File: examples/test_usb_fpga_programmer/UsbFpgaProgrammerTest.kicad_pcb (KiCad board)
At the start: 2 copper layers, 52 x 18 mm, 38 parts

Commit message: ferrite bead
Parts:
- 0FB1: renamed from 0R3; footprint Resistor_SMD:R_0603_1608Metric -> Inductor_SMD:L_0603_1608Metric
- 0FB2: renamed from 0R4; footprint Resistor_SMD:R_0603_1608Metric -> Inductor_SMD:L_0603_1608Metric
- 0FB3: renamed from 0R5; footprint Resistor_SMD:R_0603_1608Metric -> Inductor_SMD:L_0603_1608Metric
- moved 0H1 28.6 mm to (124.0, 54.0)
- moved 0H3 28.2 mm to (150.0, 42.0)
- moved 0H2 1.41 mm to (150.0, 54.0)
- renumbered 0R6 to 0R3, 0R7 to 0R4, 0R8 to 0R5, 0R9 to 0R6, 0R10 to 0R7, 0R11 to 0R8

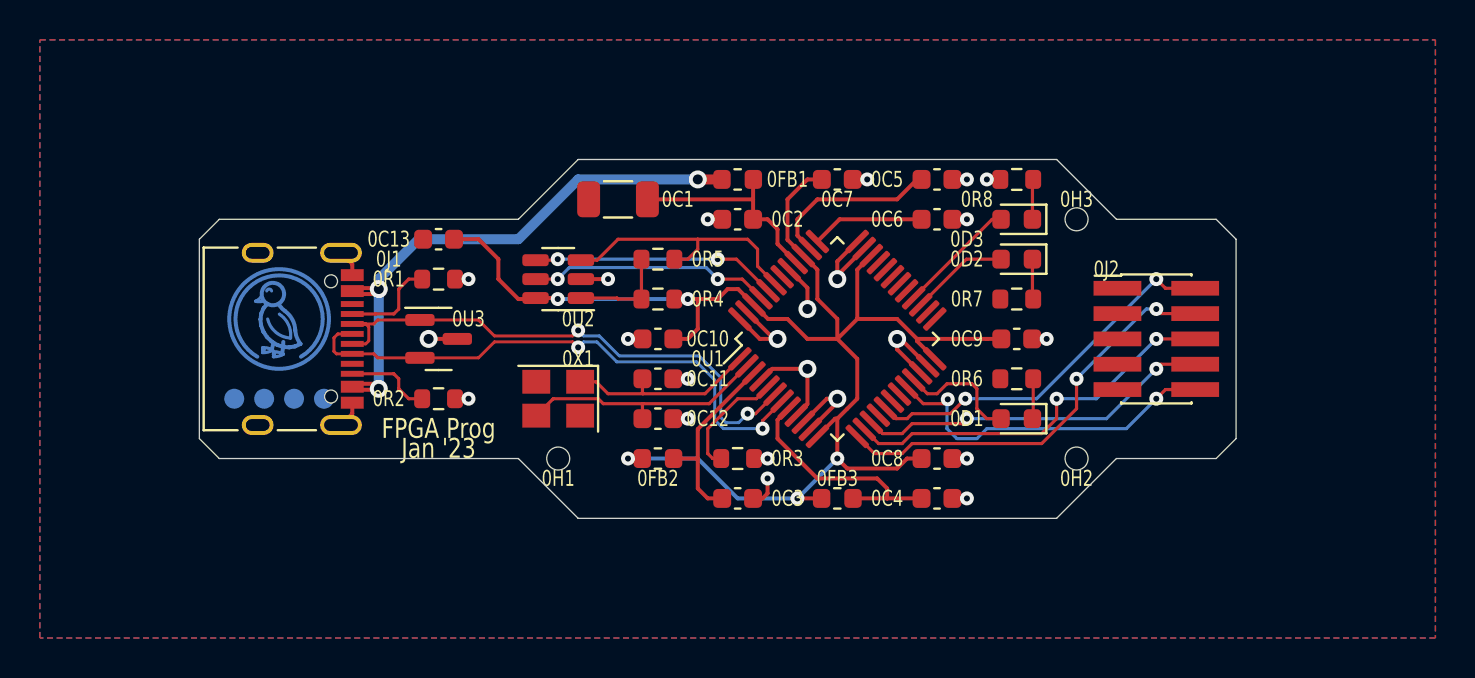
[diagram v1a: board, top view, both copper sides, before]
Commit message: leds and protection diodes
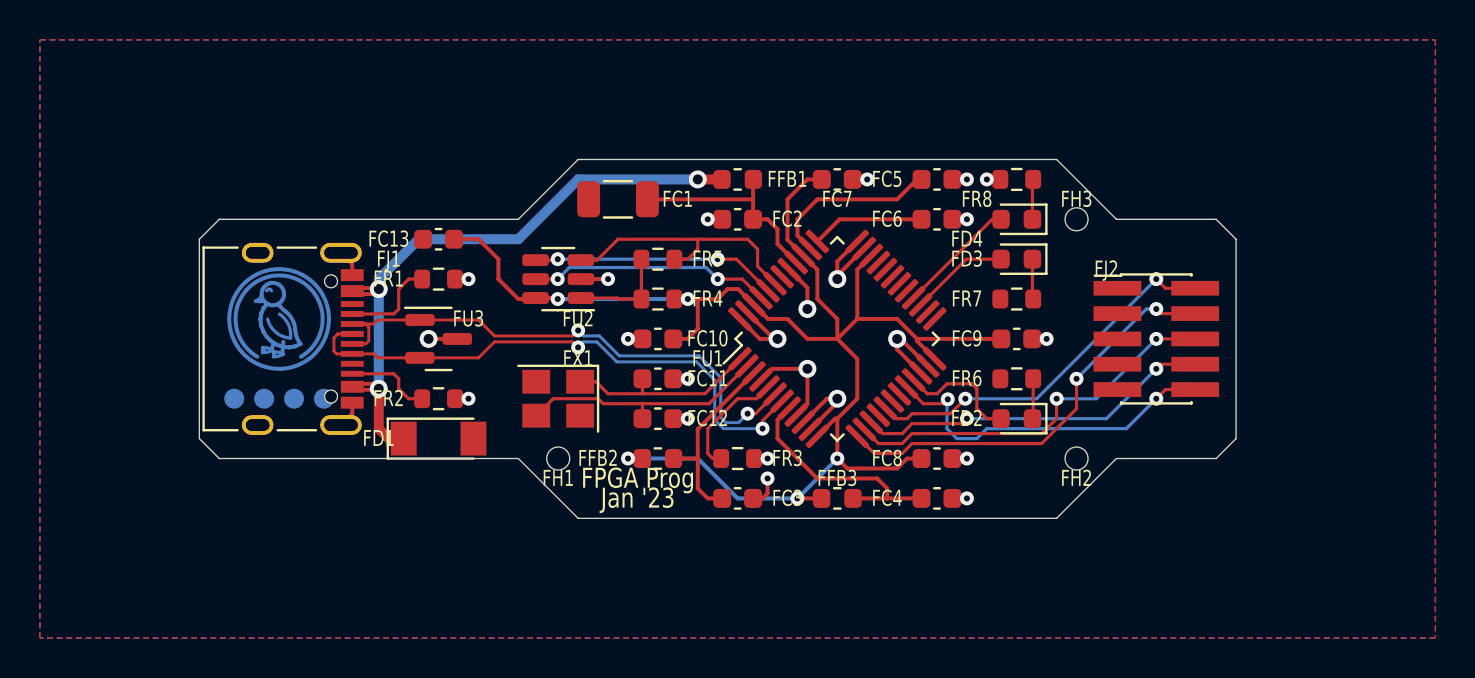
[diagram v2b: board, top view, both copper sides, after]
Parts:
- added FD1: , Diode_SMD:D_MiniMELF, F.Cu at (118.0, 53.0)
- FD2: renamed from 0D1; value KT-0603R (Hubei KENTO Elec) - Red 615~630nm 1.9~2.2V 0603 Light Emitting Diodes (LED) RoHS -> C2290 (Hubei KENTO Elec) - White 0603 Light Emitting Diodes (LED) RoHS
- FD3: renamed from 0D2; value KT-0603R (Hubei KENTO Elec) - Red 615~630nm 1.9~2.2V 0603 Light Emitting Diodes (LED) RoHS -> (none)
- renumbered 0C1 to FC1, 0C10 to FC10, 0C11 to FC11, 0C12 to FC12, 0C13 to FC13, 0C2 to FC2, 0C3 to FC3, 0C4 to FC4, 0C5 to FC5, 0C6 to FC6, 0C7 to FC7, 0C8 to FC8, 0C9 to FC9, 0D3 to FD4, 0FB1 to FFB1, 0FB2 to FFB2, 0FB3 to FFB3, 0H1 to FH1, 0H2 to FH2, 0H3 to FH3, 0J1 to FJ1, 0J2 to FJ2, 0R1 to FR1, 0R2 to FR2, 0R3 to FR3, 0R4 to FR4, 0R5 to FR5, 0R6 to FR6, 0R7 to FR7, 0R8 to FR8, 0U1 to FU1, 0U2 to FU2, 0U3 to FU3, 0U4 to FU4, 0U5 to FU5, 0X1 to FX1
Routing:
- net vusb: track 30.3 -> 33.8 mm

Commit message: clean up protection
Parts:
- FD1: value (none) -> MMSZ5232A_R1_00001 (PANJIT International) - 5?A@3V 11? Single 5.49V~5.71V 500mW 5.6V SOD-123 Zener Diodes ROHS; footprint Diode_SMD:D_MiniMELF -> Diode_SMD:D_SOD-123
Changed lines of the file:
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@@
     )
   )
-  (footprint "Diode_SMD:D_MiniMELF" (layer "F.Cu")
+  (footprint "Diode_SMD:D_SOD-123" (layer "F.Cu")
     (at 118 53)
-    (descr "Diode Mini-MELF (SOD-80)")
-    (tags "Diode Mini-MELF (SOD-80)")
+    (descr "SOD-123")
+    (tags "SOD-123")
     (property "Sheetfile" "")
     (property "Sheetname" "")
-    (property "edg_part" "TCLLZ5V6TR (Tak Cheong)")
+    (property "edg_part" "MMSZ5232A_R1_00001 (PANJIT International)")
     (property "edg_path" "vusb_protect.diode")
     (property "edg_refdes" "FD1")
@@
       (effects (font (size 0.8 0.6) (thickness 0.1)))
     )
-    (fp_text value "" (at 0 1.75) (layer "F.Fab")
+    (fp_text value "MMSZ5232A_R1_00001 (PANJIT International) - 5?A@3V 11? Single 5.49V~5.71V 500mW 5.6V SOD-123 Zener Diodes ROHS" (at 0 2.1) (layer "F.Fab")
       (effects (font (size 1 1) (thickness 0.15)))
     )
@@
       (effects (font (size 1 1) (thickness 0.15)))
     )
-    (fp_line (start 1.75 -1) (end -2.55 -1) (layer "F.SilkS") (width 0.12))
-    (fp_line (start -2.55 1) (end 1.75 1) (layer "F.SilkS") (width 0.12))
-    (fp_line (start -2.55 -1) (end -2.55 1) (layer "F.SilkS") (width 0.12))
-    (fp_line (start 2.65 -1.1) (end 2.65 1.1) (layer "F.CrtYd") (width 0.05))
-    (fp_line (start -2.65 1.1) (end -2.65 -1.1) (layer "F.CrtYd") (width 0.05))
-    (fp_line (start 2.65 1.1) (end -2.65 1.1) (layer "F.CrtYd") (width 0.05))
-    (fp_line (start -2.65 -1.1) (end 2.65 -1.1) (layer "F.CrtYd") (width 0.05))
-    (fp_line (start -1.65 -0.8) (end 1.65 -0.8) (layer "F.Fab") (width 0.1))
+    (fp_line (start -2.25 -1) (end -2.25 1) (layer "F.SilkS") (width 0.12))
+    (fp_line (start -2.25 1) (end 1.65 1) (layer "F.SilkS") (width 0.12))
+    (fp_line (start -2.25 -1) (end 1.65 -1) (layer "F.SilkS") (width 0.12))
+    (fp_line (start -2.35 -1.15) (end -2.35 1.15) (layer "F.CrtYd") (width 0.05))
+    (fp_line (start 2.35 -1.15) (end 2.35 1.15) (layer "F.CrtYd") (width 0.05))
+    (fp_line (start -2.35 -1.15) (end 2.35 -1.15) (layer "F.CrtYd") (width 0.05))
+    (fp_line (start 2.35 1.15) (end -2.35 1.15) (layer "F.CrtYd") (width 0.05))
+    (fp_line (start -1.4 -0.9) (end 1.4 -0.9) (layer "F.Fab") (width 0.1))
+    (fp_line (start -0.35 0) (end -0.35 0.55) (layer "F.Fab") (width 0.1))
+    (fp_line (start 0.25 -0.4) (end 0.25 0.4) (layer "F.Fab") (width 0.1))
+    (fp_line (start 0.25 0.4) (end -0.35 0) (layer "F.Fab") (width 0.1))
+    (fp_line (start -0.35 0) (end -0.35 -0.55) (layer "F.Fab") (width 0.1))
+    (fp_line (start 1.4 0.9) (end -1.4 0.9) (layer "F.Fab") (width 0.1))
+    (fp_line (start -1.4 0.9) (end -1.4 -0.9) (layer "F.Fab") (width 0.1))
     (fp_line (start 0.25 0) (end 0.75 0) (layer "F.Fab") (width 0.1))
+    (fp_line (start -0.75 0) (end -0.35 0) (layer "F.Fab") (width 0.1))
+    (fp_line (start 1.4 -0.9) (end 1.4 0.9) (layer "F.Fab") (width 0.1))
     (fp_line (start -0.35 0) (end 0.25 -0.4) (layer "F.Fab") (width 0.1))
-    (fp_line (start 0.25 -0.4) (end 0.25 0.4) (layer "F.Fab") (width 0.1))
-    (fp_line (start -0.35 0) (end -0.35 0.55) (layer "F.Fab") (width 0.1))
-    (fp_line (start -0.75 0) (end -0.35 0) (layer "F.Fab") (width 0.1))
-    (fp_line (start 1.65 -0.8) (end 1.65 0.8) (layer "F.Fab") (width 0.1))
-    (fp_line (start 0.25 0.4) (end -0.35 0) (layer "F.Fab") (width 0.1))
-    (fp_line (start -1.65 0.8) (end -1.65 -0.8) (layer "F.Fab") (width 0.1))
-    (fp_line (start -0.35 0) (end -0.35 -0.55) (layer "F.Fab") (width 0.1))
-    (fp_line (start 1.65 0.8) (end -1.65 0.8) (layer "F.Fab") (width 0.1))
-    (pad "1" smd rect (at -1.75 0) (size 1.3 1.7) (layers "F.Cu" "F.Paste" "F.Mask")
+    (pad "1" smd rect (at -1.65 0) (size 0.9 1.2) (layers "F.Cu" "F.Paste" "F.Mask")
       (net 3 "vusb"))
-    (pad "2" smd rect (at 1.75 0) (size 1.3 1.7) (layers "F.Cu" "F.Paste" "F.Mask")
+    (pad "2" smd rect (at 1.65 0) (size 0.9 1.2) (layers "F.Cu" "F.Paste" "F.Mask")
       (net 1 "gnd"))
-    (model "${KICAD6_3DMODEL_DIR}/Diode_SMD.3dshapes/D_MiniMELF.wrl"
+    (model "${KICAD6_3DMODEL_DIR}/Diode_SMD.3dshapes/D_SOD-123.wrl"
       (offset (xyz 0 0 0))
       (scale (xyz 1 1 1))

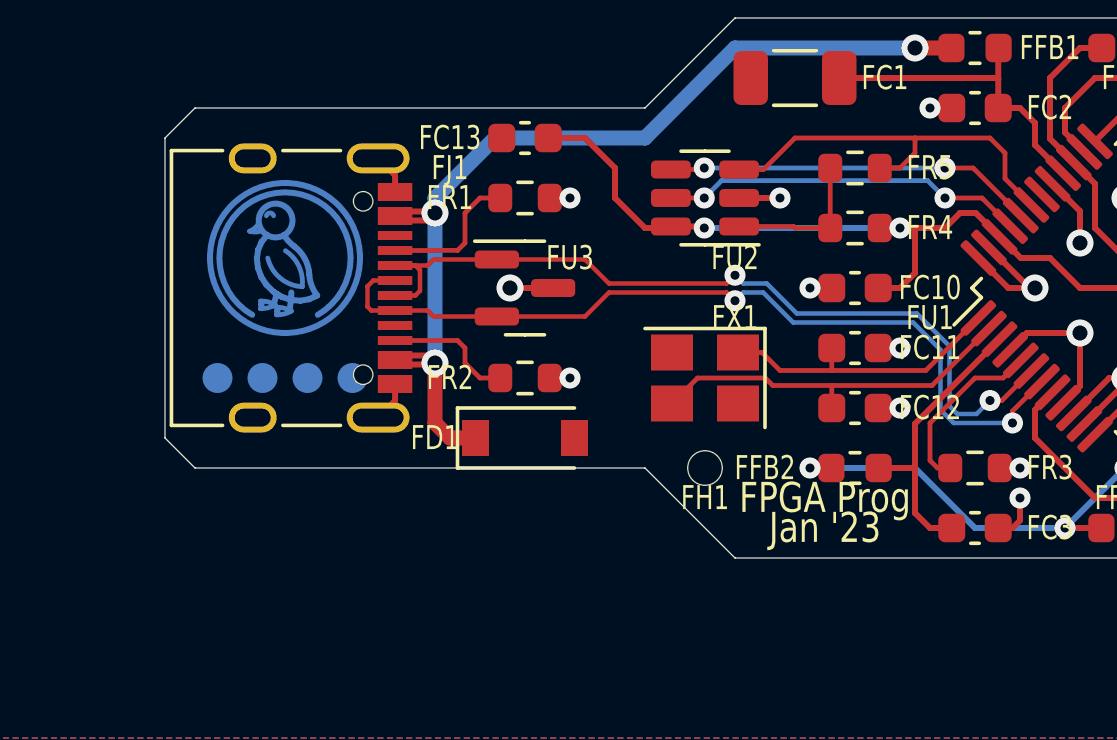
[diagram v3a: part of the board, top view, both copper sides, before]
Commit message: update board art
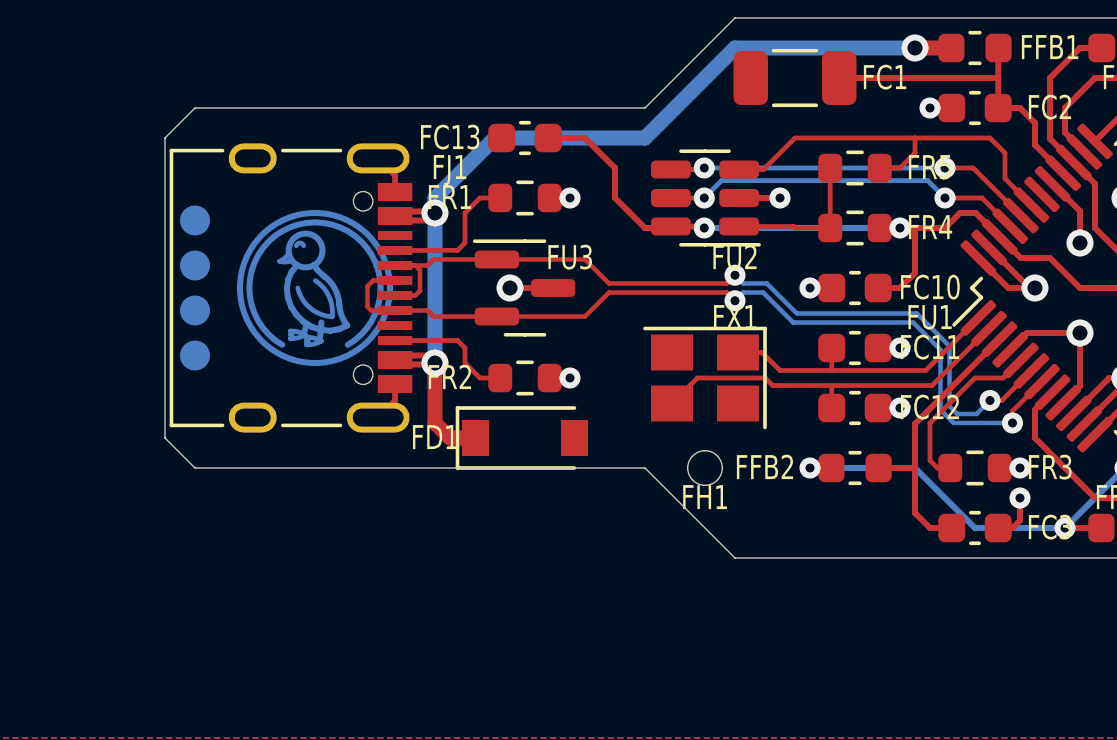
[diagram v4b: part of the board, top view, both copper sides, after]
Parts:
- added FU5: Lemur, edg:Symbol_LemurSmall, B.Cu at (116.0, 48.0)
- moved FU6 4.24 mm to (107.0, 48.0), turned to 90 degrees
- moved FU4 1.41 mm to (111.0, 48.0)
- renumbered FU5 to FU6
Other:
- board text added: "FT232 FPGA Prog Jan '23"
- board text removed: "FPGA Prog"
- board text removed: "Jan '23"

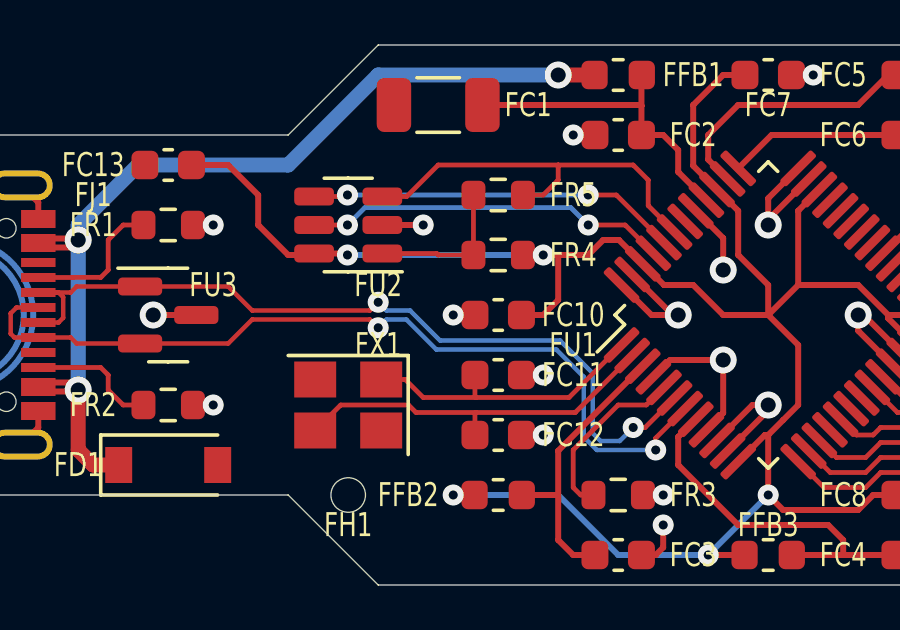
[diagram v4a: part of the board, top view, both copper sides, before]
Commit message: serpentine for length matching
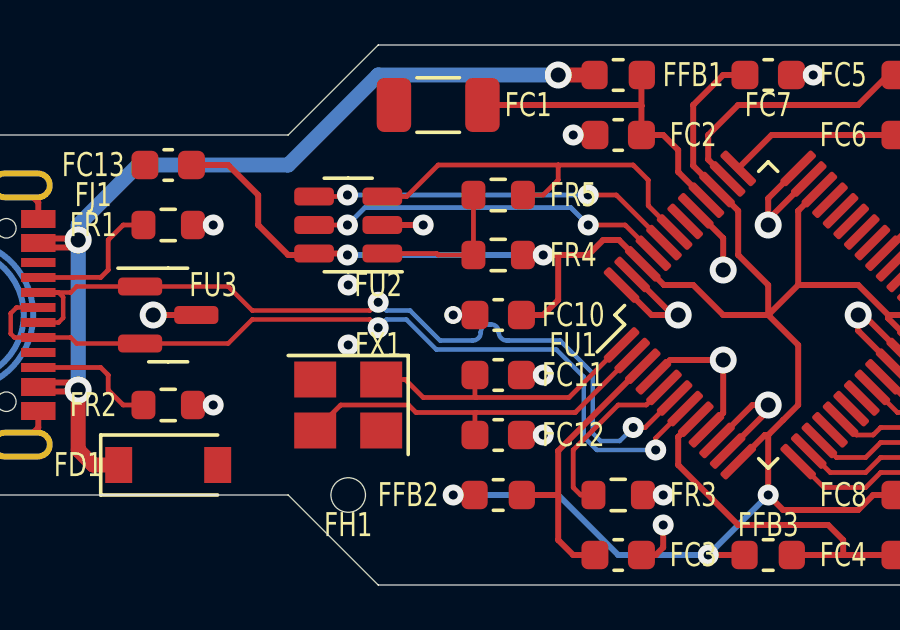
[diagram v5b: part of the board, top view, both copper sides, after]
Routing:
- net usb_chain_0.d_N: track 27.9 -> 28.5 mm
- net gnd: vias 23 -> 25
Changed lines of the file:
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@@
     (fp_arc (start -0.573812 -0.957555) (mid 0.159981 -0.670103) (end 0.575946 -0.000734) (layer "B.Cu") (width 0.16))
     (fp_arc (start 0.286757 -1.643905) (mid 0.02807 -1.671353) (end -0.213115 -1.768832) (layer "B.Cu") (width 0.16))
-    (fp_arc (start 0.763205 0.913443) (mid 0.969127 0.866758) (end 1.178844 0.891296) (layer "B.Cu") (width 0.16))
+    (fp_arc (start 0.763205 0.913443) (mid 0.969128 0.866757) (end 1.178844 0.891296) (layer "B.Cu") (width 0.16))
     (fp_arc (start 0.320058 -1.56145) (mid 0.561228 -1.658966) (end 0.819911 -1.686455) (layer "B.Cu") (width 0.16))
     (fp_arc (start -0.303506 0.391461) (mid -0.661618 -0.021387) (end -0.809366 -0.547561) (layer "B.Cu") (width 0.2))
@@
     (fp_arc (start -0.303506 0.391461) (mid -0.117368 0.560252) (end 0.03125 0.762861) (layer "B.Cu") (width 0.2))
     (fp_arc (start -1.072198 -1.25) (mid -0.886856 -0.918958) (end -0.809364 -0.547562) (layer "B.Cu") (width 0.2))
-    (fp_arc (start 0.869178 1.169286) (mid 1.000176 1.003686) (end 1.178836 0.891151) (layer "B.Cu") (width 0.16))
+    (fp_arc (start 0.869178 1.169286) (mid 1.000175 1.003684) (end 1.178836 0.891151) (layer "B.Cu") (width 0.16))
     (fp_arc (start 1.093749 -1.89443) (mid 0.000001 2.187499) (end -1.09375 -1.894429) (layer "B.Cu") (width 0.2))
     (fp_circle (center 0.3125 1.25) (end 0.875 1.25) (layer "B.Cu") (width 0.2) (fill none))
@@
   (segment (start 132.225 42) (end 131.5 42) (width 0.2) (layer "F.Cu") (net 1))
   (segment (start 133.825 54) (end 134.5 54) (width 0.16) (layer "F.Cu") (net 1))
-  (segment (start 128.225 48) (end 127.5 48) (width 0.2) (layer "F.Cu") (net 1))
   (segment (start 138 44.110912) (end 138.998788 43.112124) (width 0.2) (layer "F.Cu") (net 1))
   (segment (start 143.775 54) (end 144.5 54) (width 0.2) (layer "F.Cu") (net 1))
@@
   (segment (start 146.175 40) (end 145.5 40) (width 0.16) (layer "F.Cu") (net 1))
   (segment (start 134.110912 48) (end 133.112124 47.001212) (width 0.2) (layer "F.Cu") (net 1))
+  (segment (start 128.225 48) (end 127.5 48) (width 0.15) (layer "F.Cu") (net 1))
   (segment (start 135 48) (end 134.110912 48) (width 0.2) (layer "F.Cu") (net 1))
   (segment (start 135.586998 44.526338) (end 136.5 45.43934) (width 0.2) (layer "F.Cu") (net 1))
@@
   (via (at 134.5 54) (size 0.7) (drill 0.3) (layers "F.Cu" "B.Cu") (net 1))
   (via (at 131.5 42) (size 0.7) (drill 0.3) (layers "F.Cu" "B.Cu") (net 1))
+  (via (at 124 49) (size 0.7) (drill 0.3) (layers "F.Cu" "B.Cu") (net 1))
   (via (at 138 45) (size 0.9) (drill 0.5) (layers "F.Cu" "B.Cu") (net 1))
   (via (at 134.5 55) (size 0.7) (drill 0.3) (layers "F.Cu" "B.Cu") (net 1))
@@
   (via (at 138 51) (size 0.9) (drill 0.5) (layers "F.Cu" "B.Cu") (net 1))
   (via (at 139.5 40) (size 0.7) (drill 0.3) (layers "F.Cu" "B.Cu") (net 1))
+  (via (at 127.5 48) (size 0.6) (drill 0.3) (layers "F.Cu" "B.Cu") (net 1))
   (via (at 130.5 50) (size 0.7) (drill 0.3) (layers "F.Cu" "B.Cu") (net 1))
+  (via (at 124 47) (size 0.7) (drill 0.3) (layers "F.Cu" "B.Cu") (net 1))
   (via (at 141 48) (size 0.9) (drill 0.5) (layers "F.Cu" "B.Cu") (net 1))
-  (via (at 127.5 48) (size 0.7) (drill 0.3) (layers "F.Cu" "B.Cu") (net 1))
   (via (at 148.5 48) (size 0.7) (drill 0.3) (layers "F.Cu" "B.Cu") (net 1))
   (segment (start 120 47.05) (end 120.799999 47.849999) (width 0.15) (layer "F.Cu") (net 2))
@@
   (via (at 133.5 51.75) (size 0.7) (drill 0.3) (layers "F.Cu" "B.Cu") (net 2))
   (via (at 125 47.575) (size 0.7) (drill 0.3) (layers "F.Cu" "B.Cu") (net 2))
+  (segment (start 128.689326 48.310673) (end 128.75 48.310673) (width 0.15) (layer "B.Cu") (net 2))
+  (segment (start 131.062134 48.85) (end 132.15 49.937866) (width 0.15) (layer "B.Cu") (net 2))
+  (segment (start 133.050001 52.199999) (end 133.5 51.75) (width 0.15) (layer "B.Cu") (net 2))
   (segment (start 132.15 51.937866) (end 132.412133 52.199999) (width 0.15) (layer "B.Cu") (net 2))
-  (segment (start 127.062134 48.85) (end 131.062134 48.85) (width 0.15) (layer "B.Cu") (net 2))
-  (segment (start 126.062133 47.849999) (end 127.062134 48.85) (width 0.15) (layer "B.Cu") (net 2))
-  (segment (start 133.050001 52.199999) (end 133.5 51.75) (width 0.15) (layer "B.Cu") (net 2))
-  (segment (start 125 47.575) (end 125.274999 47.849999) (width 0.15) (layer "B.Cu") (net 2))
   (segment (start 125.274999 47.849999) (end 126.062133 47.849999) (width 0.15) (layer "B.Cu") (net 2))
   (segment (start 132.412133 52.199999) (end 133.050001 52.199999) (width 0.15) (layer "B.Cu") (net 2))
+  (segment (start 129.35 48.85) (end 131.062134 48.85) (width 0.15) (layer "B.Cu") (net 2))
   (segment (start 132.15 49.937866) (end 132.15 51.937866) (width 0.15) (layer "B.Cu") (net 2))
-  (segment (start 131.062134 48.85) (end 132.15 49.937866) (width 0.15) (layer "B.Cu") (net 2))
+  (segment (start 125 47.575) (end 125.274999 47.849999) (width 0.15) (layer "B.Cu") (net 2))
+  (segment (start 129.289326 48.85) (end 129.35 48.85) (width 0.15) (layer "B.Cu") (net 2))
+  (segment (start 128.419663 48.580337) (end 128.419663 48.580336) (width 0.15) (layer "B.Cu") (net 2))
+  (segment (start 129.019663 48.580336) (end 129.019663 48.580337) (width 0.15) (layer "B.Cu") (net 2))
+  (segment (start 126.062133 47.849999) (end 127.062134 48.85) (width 0.15) (layer "B.Cu") (net 2))
+  (segment (start 127.062134 48.85) (end 128.15 48.85) (width 0.15) (layer "B.Cu") (net 2))
+  (arc (start 128.75 48.310673) (mid 128.940681 48.389655) (end 129.019663 48.580336) (width 0.15) (layer "B.Cu") (net 2))
+  (arc (start 128.15 48.85) (mid 128.340681 48.771018) (end 128.419663 48.580337) (width 0.15) (layer "B.Cu") (net 2))
+  (arc (start 129.019663 48.580337) (mid 129.098645 48.771018) (end 129.289326 48.85) (width 0.15) (layer "B.Cu") (net 2))
+  (arc (start 128.419663 48.580336) (mid 128.498645 48.389655) (end 128.689326 48.310673) (width 0.15) (layer "B.Cu") (net 2))
   (segment (start 115 50.5) (end 114.75 50.25) (width 0.2) (layer "F.Cu") (net 3))
   (segment (start 114.95 45.45) (end 113.67 45.45) (width 0.2) (layer "F.Cu") (net 3))

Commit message: fix usb diode
ESD5V3AL exceeds USB capacitance limits
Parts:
- FU3: value ESDA5V3L (STMicroelectronics) -> PGB102ST23 (Littelfuse)
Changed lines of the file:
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@@
     (property "Sheetfile" "")
     (property "Sheetname" "")
-    (property "edg_part" "ESDA5V3L (STMicroelectronics)")
+    (property "edg_part" "PGB102ST23 (Littelfuse)")
     (property "edg_path" "usb_esd")
     (property "edg_refdes" "FU3")
@@
       (effects (font (size 0.8 0.6) (thickness 0.1)))
     )
-    (fp_text value "ESDA5V3L (STMicroelectronics)" (at 0 2.4) (layer "F.Fab")
+    (fp_text value "PGB102ST23 (Littelfuse)" (at 0 2.4) (layer "F.Fab")
       (effects (font (size 1 1) (thickness 0.15)))
     )
